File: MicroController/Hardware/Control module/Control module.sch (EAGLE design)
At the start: 0 parts

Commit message: Added first IC logic components
Added the ATXMEGA256A3 microcontroller, the CD74HC4067 16 channel (de)multiplexer and the CD4051BM 8 channel (de)multiplexer.
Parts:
- added U$1: XMEGA-A3-AU, SparkFun-Retired:XMEGA-A3-AU
- added U1: CD74HC4067SM96, SparkFun-IC-Logic:74HC4067SM96
- added U2: CD4051BM, Texas Instruments_By_element14_Batch_1:CD4051BM

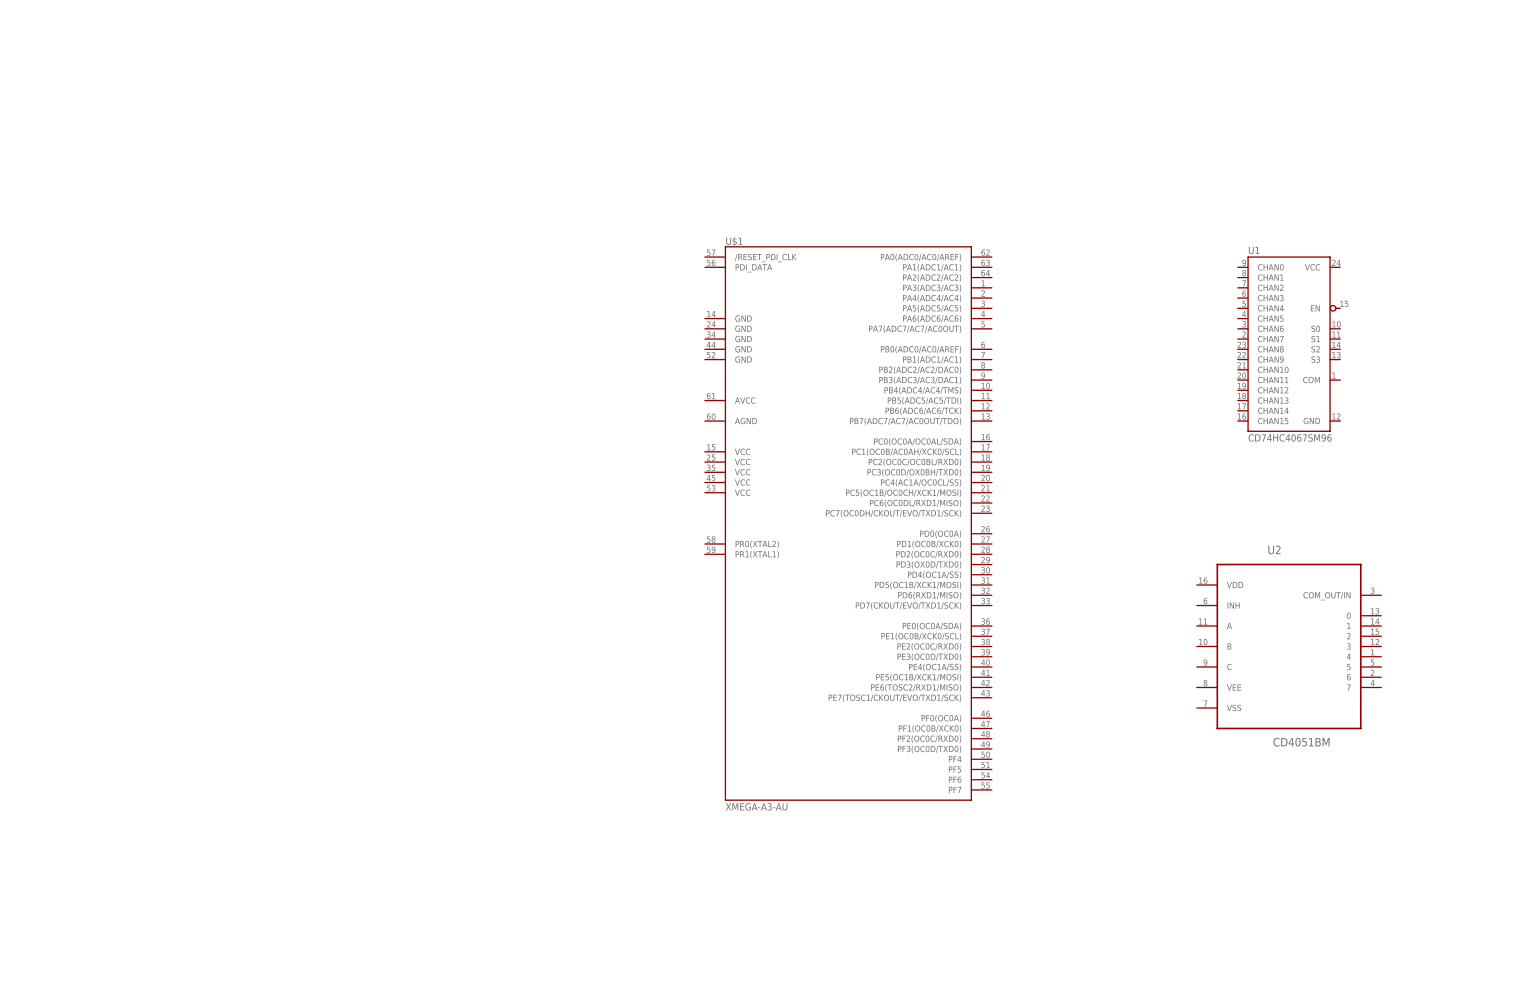
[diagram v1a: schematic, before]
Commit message: Added level shifting logic
The stepper motor drivers require a larger voltage than the microcontroller can deliver. For redundancy this voltage will be higher than 5 volts.
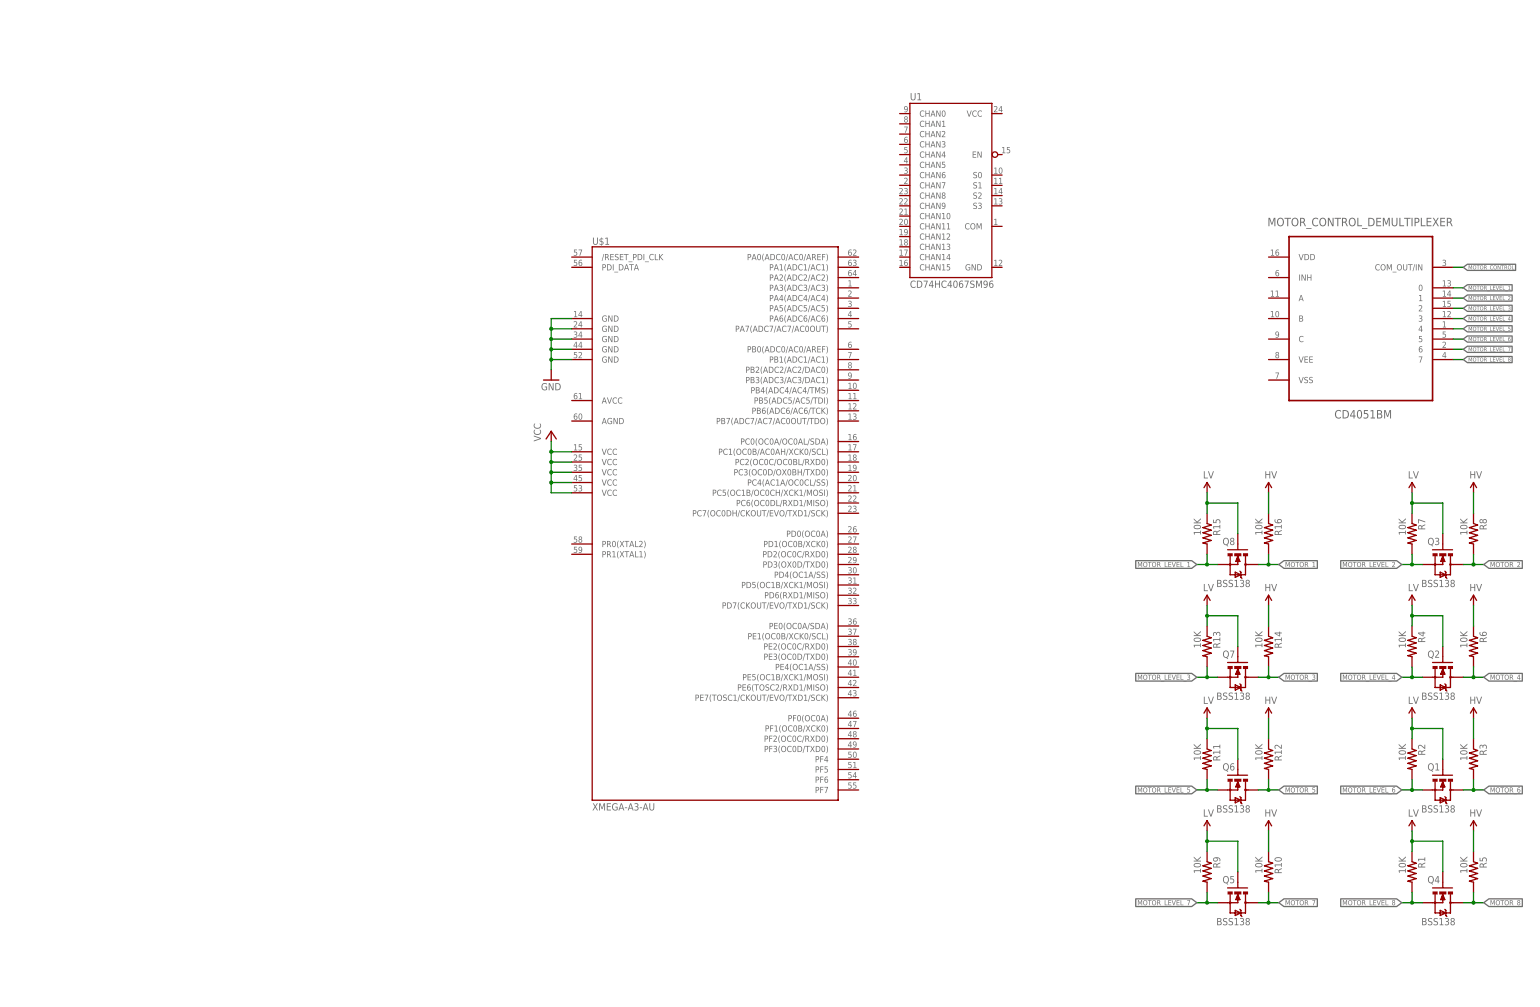
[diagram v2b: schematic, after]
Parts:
- removed U2: CD4051BM, Texas Instruments_By_element14_Batch_1:CD4051BM
- added MOTOR_CONTROL_DEMULTIPLEXER: CD4051BM, Texas Instruments_By_element14_Batch_1:CD4051BM
- added Q1, Q2, Q3, Q4, Q5, Q6, Q7, Q8: BSS138, SparkFun:MOSFET-NCHANNELSMD
- added R1, R10, R11, R12, R13, R14, R15, R16, R2, R3, R4, R5, R6, R7, R8, R9: 10K, SparkFun:RESISTOR0603-RES
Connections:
- new net GND: U$1.GND1, U$1.GND2, U$1.GND3, U$1.GND4, U$1.GND5
- new net HV: R10.1, R12.1, R14.1, R16.1, R3.1, R5.1, R6.1, R8.1
- new net LV: Q1.G, Q2.G, Q3.G, Q4.G, Q5.G, Q6.G, Q7.G, Q8.G, R1.1, R11.1, R13.1, R15.1, R2.1, R4.1, R7.1, R9.1
- new net MOTOR_1: Q8.D, R16.2
- new net MOTOR_2: Q3.D, R8.2
- new net MOTOR_3: Q7.D, R14.2
- new net MOTOR_4: Q2.D, R6.2
- new net MOTOR_5: Q6.D, R12.2
- new net MOTOR_6: Q1.D, R3.2
- new net MOTOR_7: Q5.D, R10.2
- new net MOTOR_8: Q4.D, R5.2
- new net MOTOR_CONTROL: MOTOR_CONTROL_DEMULTIPLEXER.COM_OUT/IN
- new net MOTOR_LEVEL_1: MOTOR_CONTROL_DEMULTIPLEXER.0, Q8.S, R15.2
- new net MOTOR_LEVEL_2: MOTOR_CONTROL_DEMULTIPLEXER.1, Q3.S, R7.2
- new net MOTOR_LEVEL_3: MOTOR_CONTROL_DEMULTIPLEXER.2, Q7.S, R13.2
- new net MOTOR_LEVEL_4: MOTOR_CONTROL_DEMULTIPLEXER.3, Q2.S, R4.2
- new net MOTOR_LEVEL_5: MOTOR_CONTROL_DEMULTIPLEXER.4, Q6.S, R11.2
- new net MOTOR_LEVEL_6: MOTOR_CONTROL_DEMULTIPLEXER.5, Q1.S, R2.2
- new net MOTOR_LEVEL_7: MOTOR_CONTROL_DEMULTIPLEXER.6, Q5.S, R9.2
- new net MOTOR_LEVEL_8: MOTOR_CONTROL_DEMULTIPLEXER.7, Q4.S, R1.2
- new net VCC: U$1.VCC1, U$1.VCC2, U$1.VCC3, U$1.VCC4, U$1.VCC5
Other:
- moved on the sheet: U$1, U1

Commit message: Editted the board file and added power regulating components
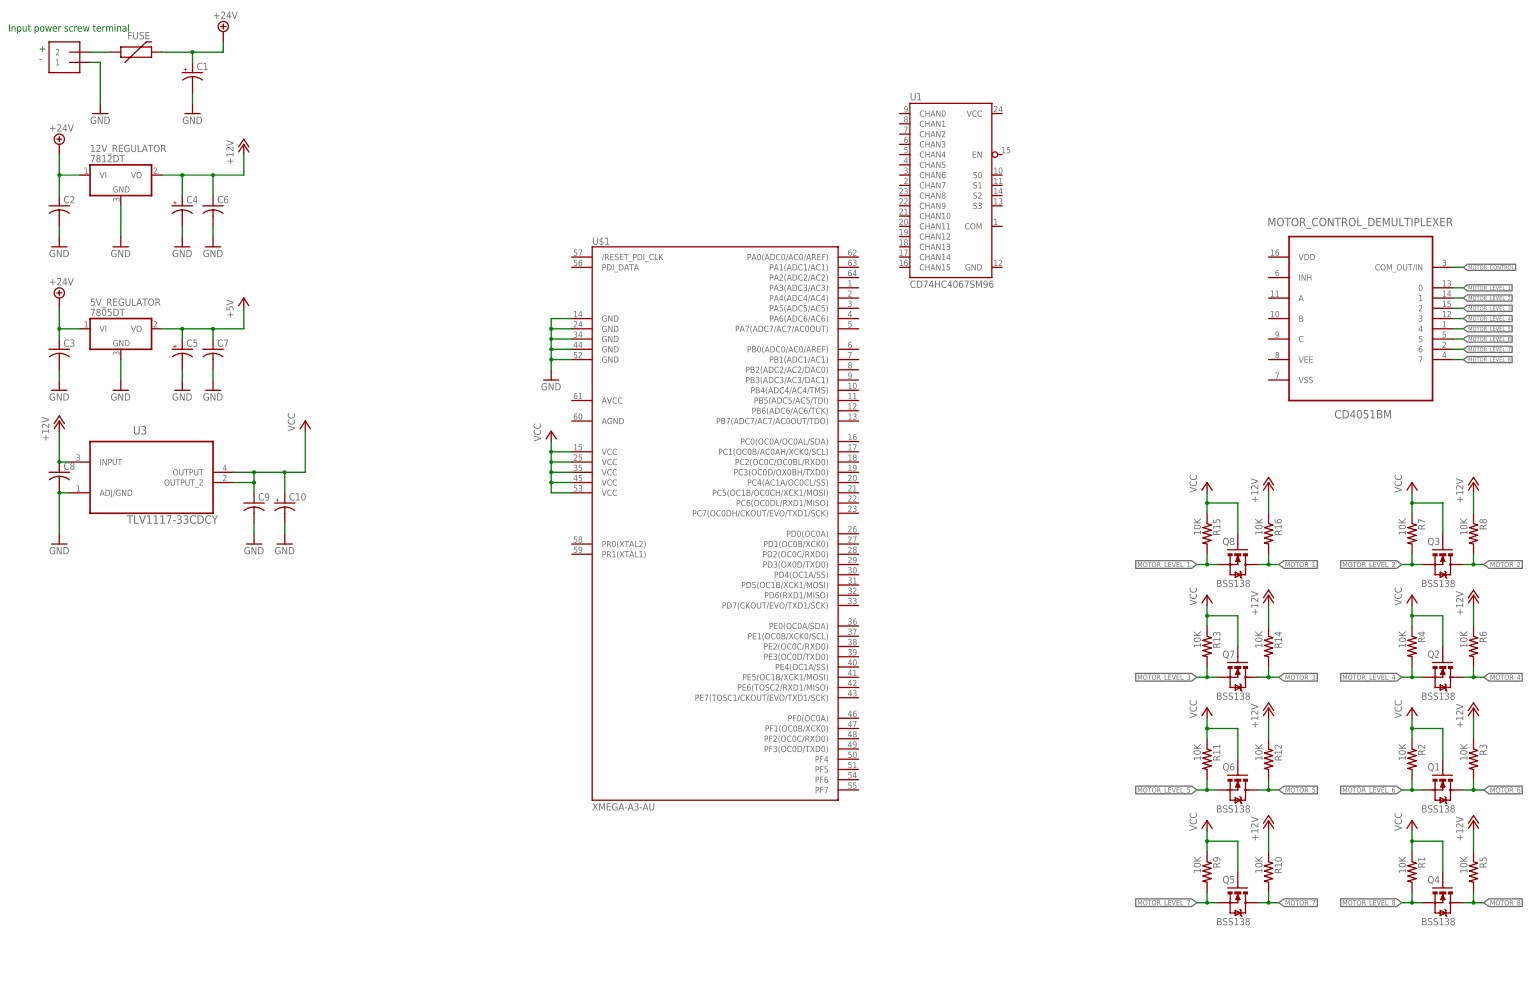
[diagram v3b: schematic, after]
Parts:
- added 12V_REGULATOR: 7812DT, adafruit:7812DT
- added 5V_REGULATOR: 7805DT, adafruit:7805DT
- added C1: (no value), adafruit:CPOL-USE5-10.5
- added C10, C4, C5: (no value), adafruit:CPOL-USE2.5-6
- added C2, C3: (no value), adafruit:C-USC1206
- added C6, C7, C8, C9: (no value), adafruit:C-USC0805
- added FUSE: 6V/0.5A, SparkFun-Fuses:PPTC_HALF-AMP
- added J1: 1X2-3.5MM, adafruit:1X2-3.5MM
- added U3: TLV1117-33CDCY, Texas Instruments_By_element14_Batch_1:TLV1117-33CDCY
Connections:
- removed net HV: R10.1, R12.1, R14.1, R16.1, R3.1, R5.1, R6.1, R8.1
- removed net LV: Q1.G, Q2.G, Q3.G, Q4.G, Q5.G, Q6.G, Q7.G, Q8.G, R1.1, R11.1, R13.1, R15.1, R2.1, R4.1, R7.1, R9.1
- new net +12V: 12V_REGULATOR.VO, C4.+, C6.1, C8.1, R10.1, R12.1, R14.1, R16.1, R3.1, R5.1, R6.1, R8.1, U3.INPUT
- new net +24V: 12V_REGULATOR.VI, 5V_REGULATOR.VI, C1.+, C2.1, C3.1, FUSE.2
- new net +5V: 5V_REGULATOR.VO, C5.+, C7.1
- new net VIN: FUSE.1, J1.2
- net GND: now also 12V_REGULATOR.GND, 5V_REGULATOR.GND, C1.-, C10.-, C2.2, C3.2, C4.-, C5.-, C6.2, C7.2, C8.2, C9.2, J1.1, U3.ADJ/GND
- net VCC: now also C10.+, C9.1, Q1.G, Q2.G, Q3.G, Q4.G, Q5.G, Q6.G, Q7.G, Q8.G, R1.1, R11.1, R13.1, R15.1, R2.1, R4.1, R7.1, R9.1, U3.OUTPUT, U3.OUTPUT_2
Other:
- note added: "+"
- note added: "-"
- note added: "Input power screw terminal"

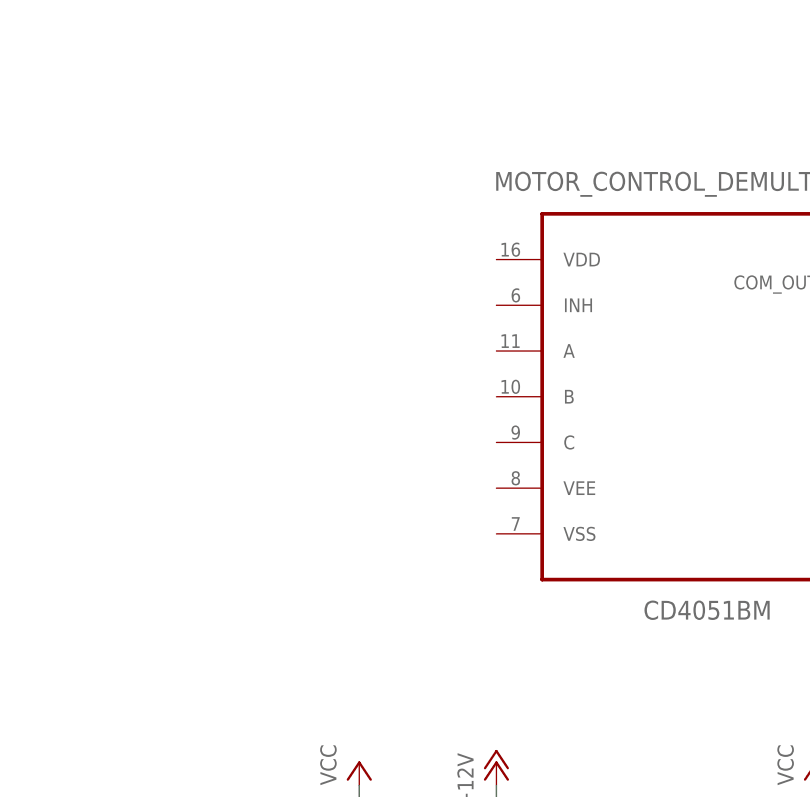
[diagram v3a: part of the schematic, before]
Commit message: Power regulation implemented on the board design
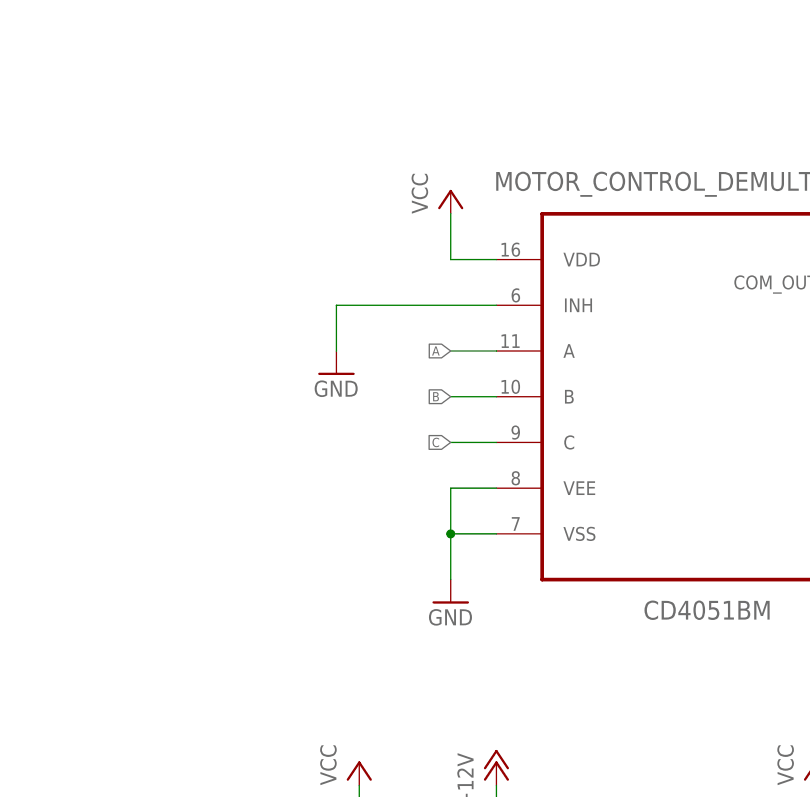
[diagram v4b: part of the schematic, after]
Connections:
- new net A: MOTOR_CONTROL_DEMULTIPLEXER.A
- new net B: MOTOR_CONTROL_DEMULTIPLEXER.B
- new net C: MOTOR_CONTROL_DEMULTIPLEXER.C
- net GND: now also MOTOR_CONTROL_DEMULTIPLEXER.INH, MOTOR_CONTROL_DEMULTIPLEXER.VEE, MOTOR_CONTROL_DEMULTIPLEXER.VSS
- net VCC: now also MOTOR_CONTROL_DEMULTIPLEXER.VDD
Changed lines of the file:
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@@
 <part name="C10" library="adafruit" library_urn="urn:adsk.eagle:library:420" deviceset="CPOL-US" device="E2.5-6"/>
 <part name="GND14" library="supply1" library_urn="urn:adsk.eagle:library:371" deviceset="GND" device=""/>
+<part name="GND15" library="supply1" library_urn="urn:adsk.eagle:library:371" deviceset="GND" device=""/>
+<part name="P+22" library="supply1" library_urn="urn:adsk.eagle:library:371" deviceset="VCC" device=""/>
+<part name="GND16" library="supply1" library_urn="urn:adsk.eagle:library:371" deviceset="GND" device=""/>
 </parts>
 <sheets>
@@
 <instance part="C10" gate="G$1" x="58.42" y="88.9"/>
 <instance part="GND14" gate="1" x="58.42" y="78.74"/>
+<instance part="GND15" gate="1" x="297.18" y="111.76"/>
+<instance part="P+22" gate="VCC" x="297.18" y="157.48"/>
+<instance part="GND16" gate="1" x="284.48" y="137.16"/>
 </instances>
 <busses>
@@
 <wire x1="58.42" y1="81.28" x2="58.42" y2="83.82" width="0.1524" layer="91"/>
 </segment>
+<segment>
+<pinref part="MOTOR_CONTROL_DEMULTIPLEXER" gate="A" pin="VSS"/>
+<pinref part="GND15" gate="1" pin="GND"/>
+<wire x1="302.26" y1="119.38" x2="297.18" y2="119.38" width="0.1524" layer="91"/>
+<wire x1="297.18" y1="119.38" x2="297.18" y2="114.3" width="0.1524" layer="91"/>
+<pinref part="MOTOR_CONTROL_DEMULTIPLEXER" gate="A" pin="VEE"/>
+<wire x1="302.26" y1="124.46" x2="297.18" y2="124.46" width="0.1524" layer="91"/>
+<wire x1="297.18" y1="124.46" x2="297.18" y2="119.38" width="0.1524" layer="91"/>
+<junction x="297.18" y="119.38"/>
+</segment>
+<segment>
+<pinref part="MOTOR_CONTROL_DEMULTIPLEXER" gate="A" pin="INH"/>
+<pinref part="GND16" gate="1" pin="GND"/>
+<wire x1="302.26" y1="144.78" x2="284.48" y2="144.78" width="0.1524" layer="91"/>
+<wire x1="284.48" y1="144.78" x2="284.48" y2="139.7" width="0.1524" layer="91"/>
+</segment>
 </net>
 <net name="VCC" class="0">
@@
 <junction x="58.42" y="96.52"/>
 </segment>
+<segment>
+<pinref part="MOTOR_CONTROL_DEMULTIPLEXER" gate="A" pin="VDD"/>
+<wire x1="302.26" y1="149.86" x2="297.18" y2="149.86" width="0.1524" layer="91"/>
+<pinref part="P+22" gate="VCC" pin="VCC"/>
+<wire x1="297.18" y1="149.86" x2="297.18" y2="154.94" width="0.1524" layer="91"/>
+</segment>
 </net>
 <net name="+12V" class="0">
@@
 </segment>
 </net>
+<net name="A" class="0">
+<segment>
+<pinref part="MOTOR_CONTROL_DEMULTIPLEXER" gate="A" pin="A"/>
+<wire x1="302.26" y1="139.7" x2="297.18" y2="139.7" width="0.1524" layer="91"/>
+<label x="297.18" y="139.7" size="1.016" layer="95" rot="R180" xref="yes"/>
+</segment>
+</net>
+<net name="B" class="0">
+<segment>
+<pinref part="MOTOR_CONTROL_DEMULTIPLEXER" gate="A" pin="B"/>
+<wire x1="302.26" y1="134.62" x2="297.18" y2="134.62" width="0.1524" layer="91"/>
+<label x="297.18" y="134.62" size="1.016" layer="95" rot="R180" xref="yes"/>
+</segment>
+</net>
+<net name="C" class="0">
+<segment>
+<pinref part="MOTOR_CONTROL_DEMULTIPLEXER" gate="A" pin="C"/>
+<wire x1="302.26" y1="129.54" x2="297.18" y2="129.54" width="0.1524" layer="91"/>
+<label x="297.18" y="129.54" size="1.016" layer="95" rot="R180" xref="yes"/>
+</segment>
+</net>

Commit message: Removed some power lines and added the IR sensor connectors
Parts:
- added J2, J3, J4: RJ45-TRAFO, con-amphenol-rj45-ld:RJ45-TRAFO
- added U$2, U$3, U$4, U$5, U$6, U$7, U$8, U$9: JST-PH_3-PIN_HEADER, SRG:JST-PH_3-PIN_HEADER
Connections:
- new net IR_1: U$6.2
- new net IR_2: U$2.2
- new net IR_3: U$7.2
- new net IR_4: U$3.2
- new net IR_5: U$8.2
- new net IR_6: U$4.2
- new net IR_7: U$9.2
- new net IR_8: U$5.2
- net GND: now also J2.GND, J2.GND1, J2.GND2, J3.GND, J3.GND1, J3.GND2, J4.GND, J4.GND1, J4.GND2, U$2.3, U$3.3, U$4.3, U$5.3, U$6.3, U$7.3, U$8.3, U$9.3
- net VCC: now also U$2.1, U$3.1, U$4.1, U$5.1, U$6.1, U$7.1, U$8.1, U$9.1
